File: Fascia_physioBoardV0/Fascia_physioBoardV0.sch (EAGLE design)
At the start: 81 parts, among them CN2 CA0612KRX7R9BB102, CN3 CA0612KRX7R9BB102, CN4 CA0612KRX7R9BB102, CN5 CA0612KRX7R9BB102, CN6 CA0612KRX7R9BB102, J1 MOLEX_52437-2471MOLEX_52437-2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, J2 MOLEX_52435-2271MOLEX_52435-2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, U1 ADS1299-X, U10 TPD4E1B06DCKR, U11 TPD4E1B06DCKR, U12 OPA320AIDBVRDBV5-L, U2 OPA2320AIDGKT_NOVA8-SOIC-L, U3 OPA2320AIDGKT_NOVAL8-SOIC-L, U4 HCNR200-300E, U5 OPA320AIDBVRDBV5-L, U6 TPD4E1B06DCKR, U7 TPD4E1B06DCKR, U8 TPD4E1B06DCKR, U9 TPD4E1B06DCKR

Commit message: minor updates
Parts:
- removed SUPPLY1: 2PT_GND_TIE, SparkFun-PowerSymbols:2PT_GND_TIE
- added C41, C64: 10uF, SparkFun-Capacitors:10UF-0603-6.3V-20%
- added C49: 0.1uF, novaXR:0.1UF-0402T-16V-10%
- added C51: 0.22uF, novaXR:0.22UF-0402T-16V-10%
- added L1, L2: BLM15HD182SN1D, SamacSys_Parts:BLM15HD182SN1D
- added U13: ADUM5028, novaXR:ADUM5028
- J2: value MOLEX_52435-2271MOLEX_52435-2271_0_0 -> MOLEX_52437-2471MOLEX_52437-2471_0_0; device Molex - 52435-2271:MOLEX_52435-2271MOLEX_52435-2271_0_0 -> Molex - 52437-2471:MOLEX_52437-2471MOLEX_52437-2471_0_0
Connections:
- new net N$6: C51.2, L1.1, U13.VISO
- net AGND: now also J2.17, J2.18; no longer SUPPLY1.P$1
- net AVDD: now also J2.21, J2.22
- net AVSS: now also J2.19, J2.20
- net BIAS_INV: now also J2.24
- net DVDD: now also C41.2, C49.2, J2.15, U13.VDDP; no longer J2.17
- net DVDD_ISO: now also C64.2, L1.2; no longer J2.20, J2.21
- net GND: now also C41.1, C49.1, J2.10, J2.11, U13.GND, U13.GND1, U13.PDIS; no longer J2.13, J2.8, J2.9, SUPPLY1.P$2
- net GND_ISO: now also C51.1, C64.1, L2.1, L2.2, U13.GND-ISO, U13.GND-ISO1, U13.VSEL; no longer J2.18, J2.19
- net PA02_EDA_SIG: now also J2.23
- net S0_I2C_SCL: now also J2.9; no longer J2.11
- net S0_I2C_SDA: now also J2.8; no longer J2.10
- net VCC: now also J2.13; no longer J2.15
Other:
- note added: "ADUM5028"

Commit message: minor updates
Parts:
- added J3: MOLEX_51296-1294MOLEX_51296-1294_0_0, Molex - 51296-1294:MOLEX_51296-1294MOLEX_51296-1294_0_0
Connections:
- net 1N: now also J1.14; no longer J1.20
- net 1P: now also J1.15; no longer J1.21
- net 2N: now also J1.12; no longer J1.18
- net 2P: now also J1.13; no longer J1.19
- net 3N: now also J1.10; no longer J1.16
- net 3P: now also J1.11; no longer J1.17
- net 4N: now also J1.8; no longer J1.14
- net 4P: now also J1.9; no longer J1.15
- net 5N: now also J1.6; no longer J1.12
- net 5P: now also J1.7; no longer J1.13
- net 6N: now also J1.4; no longer J1.10
- net 6P: now also J1.5; no longer J1.11
- net 7N: now also J3.3; no longer J1.8
- net 7P: no longer J1.9
- net 8N: now also J3.9; no longer J1.6
- net 8P: no longer J1.7
- net AGND: now also J1.16, J1.17, J1.18, J3.10, J3.4; no longer J1.24
- net AVDD: now also J3.11, J3.12, J3.5, J3.6
- net AVSS: now also J3.1, J3.2, J3.7, J3.8
- net BIAS: now also J1.3; no longer J1.5
- net GND: now also J1.19, J1.20; no longer J1.4
- net S0_I2C_SCL: now also J1.23; no longer J1.22
- net S0_I2C_SDA: now also J1.24; no longer J1.23
- net VCC: now also J1.21, J1.22; no longer J1.3

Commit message: minor changes
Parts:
- R7: value 39K -> 20K; device novaXR:39K -> novaXR:20K
- R8: value 150K -> 140K; device novaXR:150K -> novaXR:140K
- R9: value 2M -> 875K; device novaXR:2M -> novaXR:875K
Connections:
- net 7N: now also J3.9; no longer J3.3
- net 8N: now also J3.3; no longer J3.9
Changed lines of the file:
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@@
 <part name="C24" library="novaXR" deviceset="0.1UF" device="-0402T-16V-10%" value="0.1uF"/>
 <part name="C25" library="novaXR" deviceset="0.1UF" device="-0402T-16V-10%" value="0.1uF"/>
-<part name="R7" library="novaXR" deviceset="39K" device="" value="39K"/>
-<part name="R8" library="novaXR" deviceset="150K" device="" value="150K"/>
+<part name="R7" library="novaXR" deviceset="20K" device="" value="20K"/>
+<part name="R8" library="novaXR" deviceset="140K" device="" value="140K"/>
 <part name="C26" library="novaXR" deviceset="1UF" device="-0402T-16V-10%" value="1uF"/>
 <part name="U$29" library="supply1" deviceset="GND_ISO" device=""/>
@@
 <part name="U$31" library="supply1" deviceset="GND_ISO" device=""/>
 <part name="U$19" library="supply1" deviceset="DVDD_ISO" device=""/>
-<part name="R9" library="novaXR" deviceset="2M" device="" value="2M"/>
+<part name="R9" library="novaXR" deviceset="875K" device="" value="875K"/>
 <part name="R10" library="novaXR" deviceset="75K" device="" value="75K"/>
 <part name="R11" library="novaXR" deviceset="150K" device="" value="150K"/>
@@
 </segment>
 <segment>
-<wire x1="233.5784" y1="170.18" x2="228.6" y2="170.18" width="0.1524" layer="91"/>
-<label x="234.696" y="170.18" size="1.016" layer="95" xref="yes"/>
-<wire x1="228.6" y1="170.18" x2="234.696" y2="170.18" width="0.1524" layer="91"/>
-<junction x="228.6" y="170.18"/>
-<pinref part="J3" gate="G$0" pin="3"/>
+<wire x1="233.5784" y1="185.42" x2="228.6" y2="185.42" width="0.1524" layer="91"/>
+<label x="234.696" y="185.42" size="1.016" layer="95" xref="yes"/>
+<wire x1="228.6" y1="185.42" x2="234.696" y2="185.42" width="0.1524" layer="91"/>
+<junction x="228.6" y="185.42"/>
+<pinref part="J3" gate="G$0" pin="9"/>
 </segment>
 </net>
@@
 </segment>
 <segment>
-<wire x1="233.5784" y1="185.42" x2="228.6" y2="185.42" width="0.1524" layer="91"/>
-<label x="234.696" y="185.42" size="1.016" layer="95" xref="yes"/>
-<wire x1="228.6" y1="185.42" x2="234.696" y2="185.42" width="0.1524" layer="91"/>
-<junction x="228.6" y="185.42"/>
-<pinref part="J3" gate="G$0" pin="9"/>
-</segment>
-</net>
+<wire x1="233.5784" y1="170.18" x2="228.6" y2="170.18" width="0.1524" layer="91"/>
+<label x="234.696" y="170.18" size="1.016" layer="95" xref="yes"/>
+<wire x1="228.6" y1="170.18" x2="234.696" y2="170.18" width="0.1524" layer="91"/>
+<junction x="228.6" y="170.18"/>
+<pinref part="J3" gate="G$0" pin="3"/>
+</segment>
+</net>

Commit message: minor updates
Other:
- note removed: "OPENBCI"
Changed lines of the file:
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@@
 <wire x1="327.66" y1="124.46" x2="327.66" y2="100.24" width="0.1524" layer="94"/>
 <wire x1="327.66" y1="100.24" x2="429.26" y2="100.24" width="0.1524" layer="94"/>
-<text x="332.74" y="25.4" size="5.08" layer="97">OPENBCI </text>
 <text x="198.12" y="53.34" size="2.1844" layer="95">ADUM5028</text>
 </plain>

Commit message: minor layout changes
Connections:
- net AVDD: now also U11.IO2
- net VCC: no longer U11.IO2
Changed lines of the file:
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@@
 <pinref part="J3" gate="G$0" pin="12"/>
+</segment>
+<segment>
+<pinref part="U11" gate="G$1" pin="IO2"/>
+<wire x1="80.01" y1="17.78" x2="76.454" y2="17.78" width="0.1524" layer="91"/>
+<label x="76.454" y="17.78" size="1.778" layer="95" rot="R180" xref="yes"/>
 </segment>
 </net>
@@
 </segment>
 <segment>
-<pinref part="U11" gate="G$1" pin="IO2"/>
-<wire x1="80.01" y1="17.78" x2="76.454" y2="17.78" width="0.1524" layer="91"/>
-<label x="76.454" y="17.78" size="1.778" layer="95" rot="R180" xref="yes"/>
-</segment>
-<segment>

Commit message: wiring progress
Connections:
- removed net PA07_DRDY2: J2.2, U1.!DRDY
- new net PA07_DRDY: J2.7, U1.!DRDY
- net ADS_CLK: now also J2.3; no longer J2.1
- net ADS_RESET2: now also J2.2; no longer J2.5
- net PA16_S1_MOSI: now also J2.1; no longer J2.4
- net PA17_S1_SCK: now also J2.5; no longer J2.6
- net PA19_S1_MISO: now also J2.6; no longer J2.7
- net PA20_CS2: now also J2.4; no longer J2.3
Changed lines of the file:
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@@
 </segment>
 <segment>
-<wire x1="157.48" y1="152.4" x2="172.72" y2="152.4" width="0.1524" layer="91"/>
-<label x="172.72" y="152.4" size="1.016" layer="95" xref="yes"/>
-<pinref part="J2" gate="G$0" pin="7"/>
+<pinref part="J2" gate="G$0" pin="6"/>
+<wire x1="157.48" y1="149.86" x2="172.72" y2="149.86" width="0.1524" layer="91"/>
+<label x="172.72" y="149.86" size="1.016" layer="95" xref="yes"/>
 </segment>
 </net>
@@
 </segment>
 <segment>
-<wire x1="157.48" y1="149.86" x2="172.72" y2="149.86" width="0.1524" layer="91"/>
-<label x="172.72" y="149.86" size="1.016" layer="95" xref="yes"/>
-<pinref part="J2" gate="G$0" pin="6"/>
+<label x="172.72" y="147.32" size="1.016" layer="95" xref="yes"/>
+<wire x1="162.56" y1="147.32" x2="172.72" y2="147.32" width="0.1524" layer="91"/>
+<pinref part="J2" gate="G$0" pin="5"/>
+<wire x1="157.48" y1="147.32" x2="162.56" y2="147.32" width="0.1524" layer="91"/>
 </segment>
 </net>
@@
 </segment>
 <segment>
-<wire x1="157.48" y1="144.78" x2="172.72" y2="144.78" width="0.1524" layer="91"/>
-<label x="172.72" y="144.78" size="1.016" layer="95" xref="yes"/>
-<pinref part="J2" gate="G$0" pin="4"/>
+<label x="172.72" y="137.16" size="1.016" layer="95" xref="yes"/>
+<wire x1="162.56" y1="137.16" x2="172.72" y2="137.16" width="0.1524" layer="91"/>
+<pinref part="J2" gate="G$0" pin="1"/>
+<wire x1="157.48" y1="137.16" x2="162.56" y2="137.16" width="0.1524" layer="91"/>
 </segment>
 </net>
@@
 </segment>
 <segment>
-<wire x1="157.48" y1="142.24" x2="172.72" y2="142.24" width="0.1524" layer="91"/>
-<label x="172.72" y="142.24" size="1.016" layer="95" xref="yes"/>
-<pinref part="J2" gate="G$0" pin="3"/>
+<label x="172.72" y="144.78" size="1.016" layer="95" xref="yes"/>
+<wire x1="162.56" y1="144.78" x2="172.72" y2="144.78" width="0.1524" layer="91"/>
+<pinref part="J2" gate="G$0" pin="4"/>
+<wire x1="157.48" y1="144.78" x2="162.56" y2="144.78" width="0.1524" layer="91"/>
 </segment>
 </net>
@@
 </segment>
 <segment>
-<wire x1="157.48" y1="137.16" x2="172.72" y2="137.16" width="0.1524" layer="91"/>
-<label x="172.72" y="137.16" size="1.016" layer="95" xref="yes"/>
-<pinref part="J2" gate="G$0" pin="1"/>
-</segment>
-</net>
-<net name="PA07_DRDY2" class="0">
-<segment>
-<wire x1="157.48" y1="139.7" x2="172.72" y2="139.7" width="0.1524" layer="91"/>
-<label x="172.72" y="139.7" size="1.016" layer="95" xref="yes"/>
-<pinref part="J2" gate="G$0" pin="2"/>
-</segment>
-<segment>
-<pinref part="U1" gate="G$1" pin="!DRDY"/>
-<wire x1="372.11" y1="200.66" x2="383.286" y2="200.66" width="0.1524" layer="91"/>
-<label x="383.286" y="200.66" size="1.27" layer="95" xref="yes"/>
+<label x="172.72" y="142.24" size="1.016" layer="95" xref="yes"/>
+<wire x1="162.56" y1="142.24" x2="172.72" y2="142.24" width="0.1524" layer="91"/>
+<pinref part="J2" gate="G$0" pin="3"/>
+<wire x1="157.48" y1="142.24" x2="162.56" y2="142.24" width="0.1524" layer="91"/>
 </segment>
 </net>
@@
 <net name="ADS_RESET2" class="0">
 <segment>
-<wire x1="157.48" y1="147.32" x2="172.72" y2="147.32" width="0.1524" layer="91"/>
-<label x="172.72" y="147.32" size="1.016" layer="95" xref="yes"/>
-<pinref part="J2" gate="G$0" pin="5"/>
+<label x="172.72" y="139.7" size="1.016" layer="95" xref="yes"/>
+<wire x1="162.56" y1="139.7" x2="172.72" y2="139.7" width="0.1524" layer="91"/>
+<pinref part="J2" gate="G$0" pin="2"/>
+<wire x1="157.48" y1="139.7" x2="162.56" y2="139.7" width="0.1524" layer="91"/>
 </segment>
 <segment>
@@
 </segment>
 </net>
+<net name="PA07_DRDY" class="0">
+<segment>
+<wire x1="157.48" y1="152.4" x2="172.72" y2="152.4" width="0.1524" layer="91"/>
+<label x="172.72" y="152.4" size="1.016" layer="95" xref="yes"/>
+<pinref part="J2" gate="G$0" pin="7"/>
+</segment>
+<segment>
+<pinref part="U1" gate="G$1" pin="!DRDY"/>
+<wire x1="372.11" y1="200.66" x2="383.286" y2="200.66" width="0.1524" layer="91"/>
+<label x="383.286" y="200.66" size="1.27" layer="95" xref="yes"/>
+</segment>
+</net>

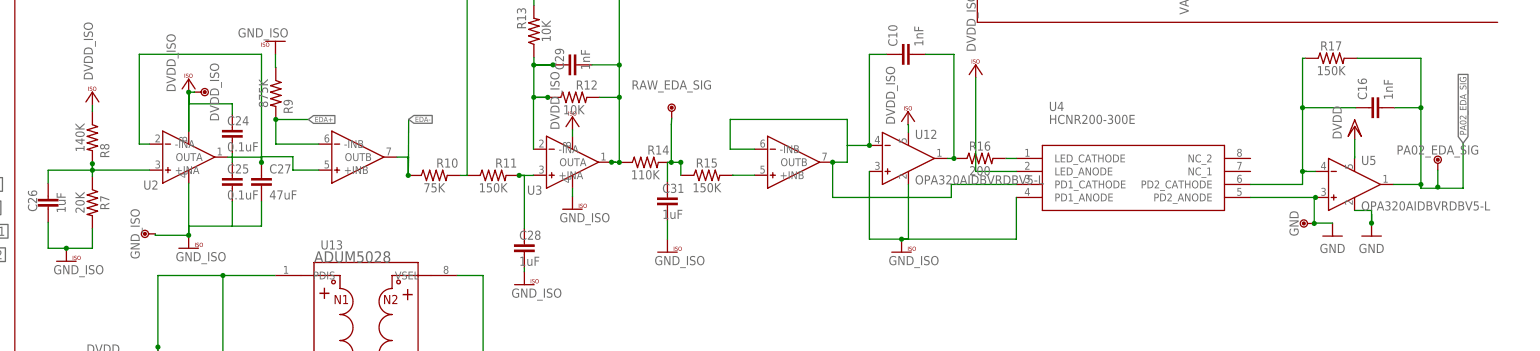
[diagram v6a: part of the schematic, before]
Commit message: fixed some traces and completed board traces
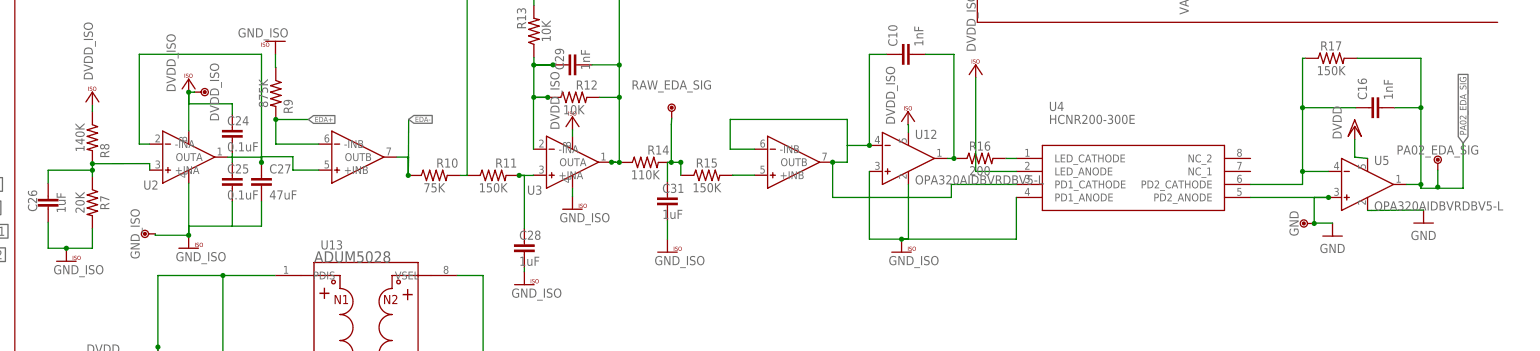
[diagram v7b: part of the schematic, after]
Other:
- moved on the sheet: U5
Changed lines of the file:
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@@
 <attribute name="VALUE" x="415.29" y="167.132" size="1.778" layer="96" align="top-center"/>
 </instance>
-<instance part="GND3" gate="1" x="404.638" y="58.496" smashed="yes">
-<attribute name="VALUE" x="404.638" y="56.972" size="1.778" layer="96" align="top-center"/>
+<instance part="GND3" gate="1" x="414.798" y="61.036" smashed="yes">
+<attribute name="VALUE" x="414.798" y="59.512" size="1.778" layer="96" align="top-center"/>
 </instance>
 <instance part="U$1" gate="G$1" x="401.352" y="77.37" smashed="yes">
@@
 <attribute name="VALUE" x="254.95" y="80.54" size="1.778" layer="96" display="off"/>
 </instance>
-<instance part="U5" gate="A" x="398.78" y="68.58" smashed="yes">
-<attribute name="NAME" x="402.59" y="72.39" size="1.778" layer="95"/>
-<attribute name="VALUE" x="402.59" y="63.5" size="1.778" layer="96"/>
+<instance part="U5" gate="A" x="401.32" y="68.58" smashed="yes">
+<attribute name="NAME" x="405.13" y="72.39" size="1.778" layer="95"/>
+<attribute name="VALUE" x="405.13" y="63.5" size="1.778" layer="96"/>
 </instance>
 <instance part="U12" gate="A" x="311.658" y="73.66" smashed="yes">
@@
 <pinref part="U$1" gate="G$1" pin="DVDD"/>
 <pinref part="U5" gate="A" pin="V+"/>
-<wire x1="401.32" y1="73.66" x2="401.352" y2="73.914" width="0.1524" layer="91"/>
+<wire x1="403.86" y1="73.66" x2="401.352" y2="73.914" width="0.1524" layer="91"/>
 <wire x1="401.352" y1="73.914" x2="401.352" y2="77.37" width="0.1524" layer="91"/>
 </segment>
@@
 <segment>
 <pinref part="GND3" gate="1" pin="GND"/>
-<wire x1="404.638" y1="61.036" x2="404.66" y2="61.036" width="0.1524" layer="91"/>
-<wire x1="404.66" y1="61.036" x2="404.66" y2="62.76" width="0.1524" layer="91"/>
 <pinref part="U5" gate="A" pin="V-"/>
-<wire x1="401.32" y1="63.5" x2="404.638" y2="63.5" width="0.1524" layer="91"/>
-<wire x1="404.638" y1="63.5" x2="404.638" y2="61.036" width="0.1524" layer="91"/>
-<junction x="404.638" y="61.036"/>
+<wire x1="403.86" y1="63.5" x2="404.638" y2="63.5" width="0.1524" layer="91"/>
+<wire x1="404.638" y1="63.5" x2="414.798" y2="63.576" width="0.1524" layer="91"/>
 </segment>
 <segment>
@@
 <wire x1="393.446" y1="61.036" x2="393.446" y2="60.96" width="0.1524" layer="91"/>
 <pinref part="U4" gate="G$1" pin="PD2_ANODE"/>
-<wire x1="381" y1="66.04" x2="393.7" y2="66.04" width="0.1524" layer="91"/>
+<wire x1="381" y1="66.04" x2="396.24" y2="66.04" width="0.1524" layer="91"/>
 <pinref part="U5" gate="A" pin="IN+"/>
-<wire x1="393.7" y1="66.04" x2="393.446" y2="66.04" width="0.1524" layer="91"/>
+<wire x1="396.24" y1="66.04" x2="393.446" y2="66.04" width="0.1524" layer="91"/>
 <wire x1="393.446" y1="66.04" x2="393.446" y2="60.96" width="0.1524" layer="91"/>
-<junction x="393.7" y="66.04"/>
+<junction x="396.24" y="66.04"/>
 <junction x="393.446" y="60.96"/>
 </segment>
@@
 <junction x="154.844" y="71.36"/>
 <pinref part="U2" gate="G$1" pin="+INA"/>
-<wire x1="166.04" y1="71.38" x2="154.844" y2="71.38" width="0.1524" layer="91"/>
-<wire x1="154.844" y1="71.38" x2="154.844" y2="72.63" width="0.1524" layer="91"/>
+<wire x1="166.04" y1="71.38" x2="166.02" y2="72.65" width="0.1524" layer="91"/>
+<wire x1="166.02" y1="72.65" x2="154.844" y2="72.63" width="0.1524" layer="91"/>
 <junction x="154.844" y="72.63"/>
 </segment>
@@
 <net name="DVDD_ISO" class="0">
 <segment>
-<wire x1="173.64" y1="78.98" x2="173.64" y2="86.6" width="0.1524" layer="91"/>
 <pinref part="U$19" gate="G$1" pin="DVDD_ISO"/>
 <pinref part="DVDD_ISO" gate="G$1" pin="P$1"/>
@@
 <pinref part="U5" gate="A" pin="OUT"/>
 <wire x1="414.274" y1="68.58" x2="414.274" y2="83.566" width="0.1524" layer="91"/>
-<wire x1="408.94" y1="68.58" x2="414.274" y2="68.58" width="0.1524" layer="91"/>
+<wire x1="411.48" y1="68.58" x2="414.274" y2="68.58" width="0.1524" layer="91"/>
 <junction x="414.274" y="68.58"/>
 </segment>
@@
 <pinref part="U4" gate="G$1" pin="PD2_CATHODE"/>
 <wire x1="381" y1="68.58" x2="391.16" y2="68.58" width="0.1524" layer="91"/>
-<wire x1="391.96" y1="71.142" x2="391.16" y2="71.142" width="0.1524" layer="91"/>
 <pinref part="C16" gate="G$1" pin="1"/>
-<wire x1="391.16" y1="71.142" x2="391.16" y2="71.12" width="0.1524" layer="91"/>
 <wire x1="391.16" y1="71.12" x2="391.16" y2="68.58" width="0.1524" layer="91"/>
 <wire x1="401.574" y1="83.566" x2="391.16" y2="83.566" width="0.1524" layer="91"/>
-<wire x1="391.16" y1="83.566" x2="391.16" y2="71.142" width="0.1524" layer="91"/>
+<wire x1="391.16" y1="83.566" x2="391.16" y2="71.12" width="0.1524" layer="91"/>
 <pinref part="R17" gate="G$1" pin="1"/>
 <wire x1="391.668" y1="93.218" x2="391.16" y2="93.218" width="0.1524" layer="91"/>
@@
 <junction x="391.16" y="83.566"/>
 <pinref part="U5" gate="A" pin="IN-"/>
-<wire x1="393.7" y1="71.12" x2="391.16" y2="71.12" width="0.1524" layer="91"/>
+<wire x1="396.24" y1="71.12" x2="391.16" y2="71.12" width="0.1524" layer="91"/>
 <junction x="391.16" y="71.12"/>
 </segment>
 </net>
-<net name="N$8" class="0">
-<segment>
-<wire x1="154.8" y1="71.38" x2="154.8" y2="71.4" width="0.1524" layer="91"/>
-</segment>
-</net>

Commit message: MINOR CHANGES
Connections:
- net ADS_RESET2 renamed ADS_RESET
- net PA20_CS2 renamed PA20_CS
- net BIAS_INV: no longer J2.24
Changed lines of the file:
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@@
 <label x="313.182" y="234.188" size="1.016" layer="95" rot="R180" xref="yes"/>
-</segment>
-<segment>
-<wire x1="157.48" y1="195.58" x2="167.64" y2="195.58" width="0.1524" layer="91"/>
-<label x="167.64" y="195.58" size="1.016" layer="95" xref="yes"/>
-<pinref part="J2" gate="G$0" pin="24"/>
 </segment>
 </net>
@@
 </segment>
 </net>
-<net name="PA20_CS2" class="0">
+<net name="PA20_CS" class="0">
 <segment>
 <pinref part="U1" gate="G$1" pin="!CS"/>
@@
 </segment>
 </net>
-<net name="ADS_RESET2" class="0">
+<net name="ADS_RESET" class="0">
 <segment>
 <label x="172.72" y="139.7" size="1.016" layer="95" xref="yes"/>
